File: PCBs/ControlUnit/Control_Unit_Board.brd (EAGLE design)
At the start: 78.7 x 65.7 mm, 14 parts, among them T1 2N2222, T2 2N2222

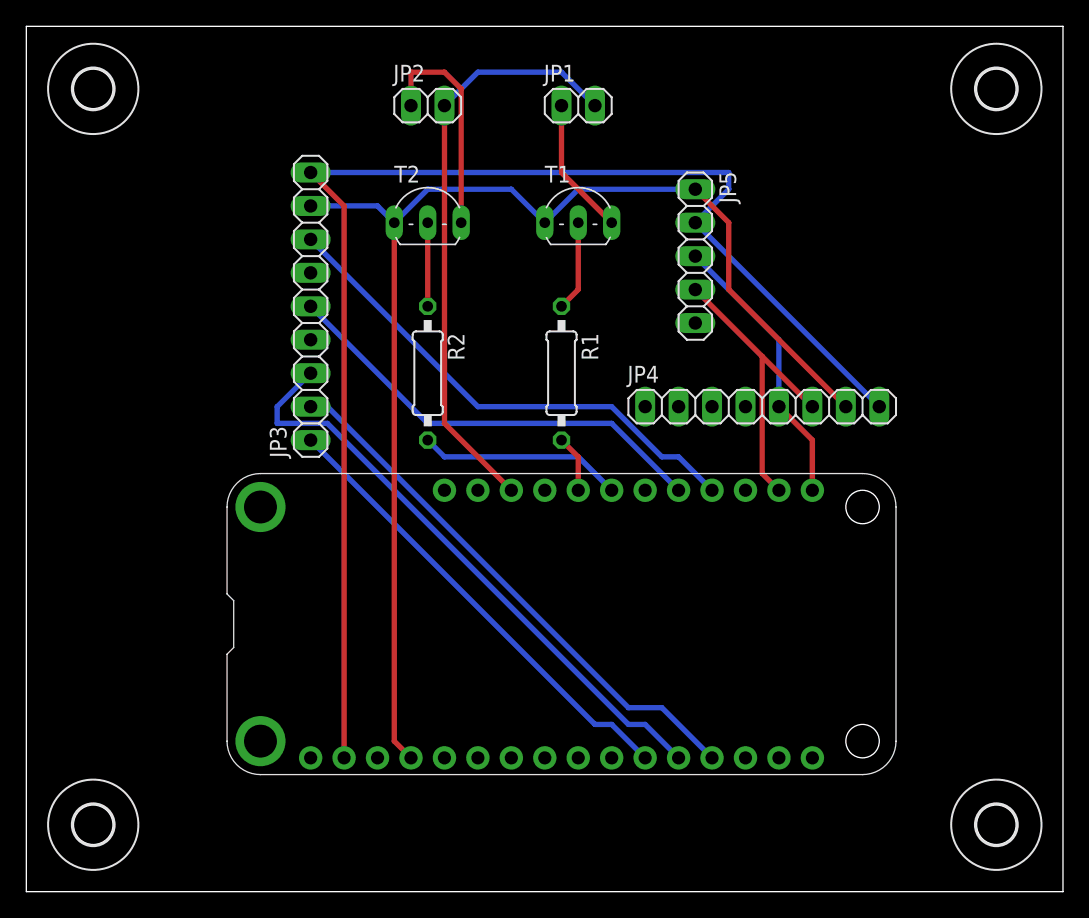
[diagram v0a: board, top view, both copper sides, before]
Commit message: Control Unit PCB finished, Sensor unit almost
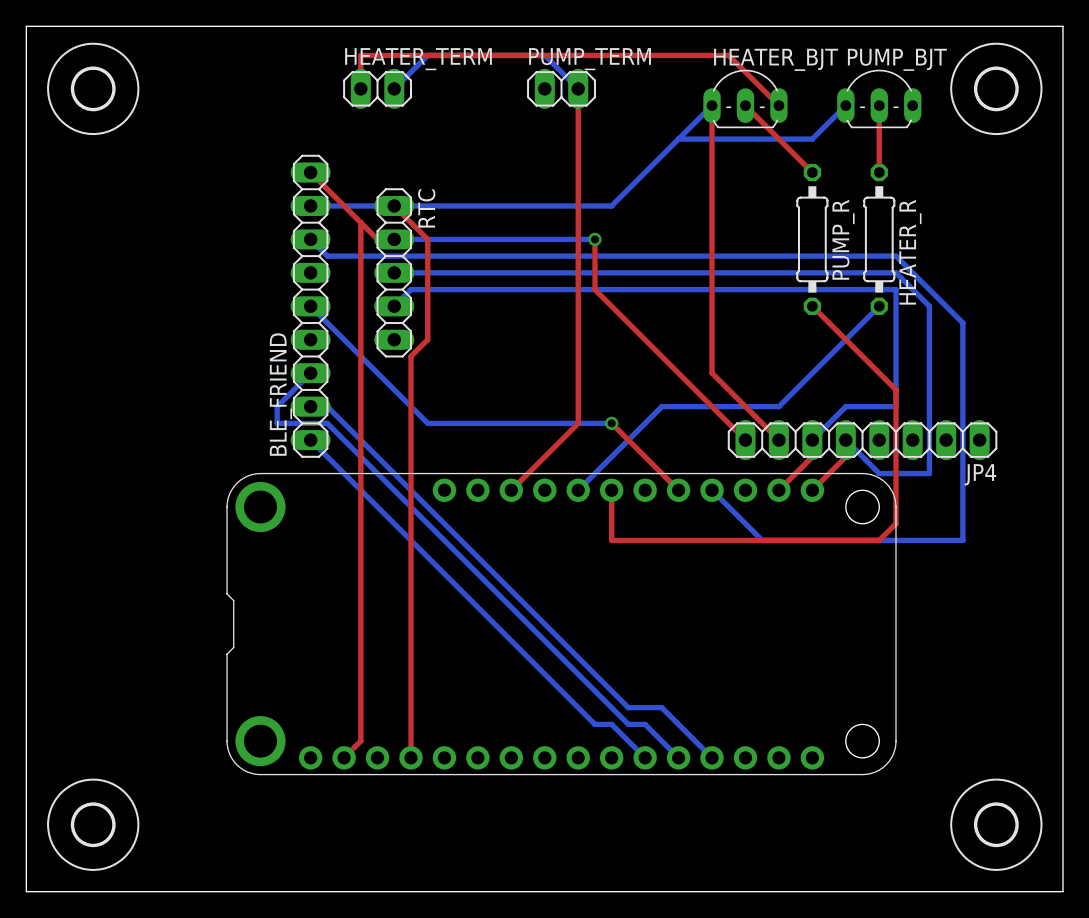
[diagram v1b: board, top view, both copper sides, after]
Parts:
- removed JP1, JP2: (no value), pinhead:1X02
- removed JP5: (no value), pinhead:1X05
- removed R1, R2: (no value), eagle-ltspice:0207/10
- removed T1, T2: 2N2222, adafruit:TO92-EBC-OVAL
- added HEATER_BJT, PUMP_BJT: 2N2222, adafruit:TO92-EBC-OVAL
- added HEATER_R, PUMP_R: (no value), eagle-ltspice:0207/10
- added HEATER_TERM, PUMP_TERM: (no value), pinhead:1X02
- added RTC: (no value), pinhead:1X05
- moved JP4 8.03 mm to (64.8, 71.1), turned to 180 degrees
- renumbered JP3 to BLE_FRIEND
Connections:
- new net S$1: PUMP_TERM.1
- net GND: now also HEATER_BJT.E, PUMP_BJT.E, RTC.1; no longer JP5.1, T1.E, T2.E
- net N$10: now also RTC.3; no longer JP5.3
- net N$11: now also PUMP_BJT.C; no longer JP1.1, T1.C
- net N$12: now also HEATER_BJT.C, HEATER_TERM.1; no longer JP2.1, T2.C
- net N$14: now also RTC.4; no longer JP5.4
- net N$6: now also PUMP_R.2; no longer R2.2
- net N$7: now also HEATER_R.2; no longer R1.2
- net N$8: now also HEATER_R.1, PUMP_BJT.B; no longer R1.1, T1.B
- net N$9: now also HEATER_BJT.B, PUMP_R.1; no longer R2.1, T2.B
- net USB: now also HEATER_TERM.2, PUMP_TERM.2; no longer JP1.2, JP2.2
- net VCC: now also RTC.2; no longer JP5.2
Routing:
- net N$15: track 38.4 -> 89.3 mm
- net N$10: track 21.5 -> 66.7 mm
- net N$14: track 23.3 -> 59.8 mm
- net N$6: track 15.5 -> 45.1 mm
- net N$7: track 4.34 -> 28.6 mm
- net GND: track 95.3 -> 118.4 mm
- net N$12: track 17.0 -> 35.9 mm
- net VCC: track 101.9 -> 84.8 mm, vias 0 -> 1
- net N$11: track 10.5 -> 0.00 mm
- net USB: track 44.8 -> 48.7 mm
- net N$8: track 6.88 -> 5.08 mm
- net N$9: track 6.35 -> 7.18 mm
- net N$5: vias 0 -> 1

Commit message: Update Control_Unit_Board.brd
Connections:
- removed net N$4: BLE_FRIEND.4
- net N$11: now also PUMP_TERM.1
- net S$1: now also BLE_FRIEND.4, MS1.22; no longer PUMP_TERM.1
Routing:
- net N$15: track 89.3 -> 53.4 mm
- net N$11: track 0.00 -> 31.6 mm
- net N$1: track 41.5 -> 72.6 mm
- net S$1: track 0.00 -> 30.1 mm
- net VCC: track 84.8 -> 108.9 mm, vias 1 -> 0
- net N$6: track 45.1 -> 28.5 mm
- net N$7: track 28.6 -> 37.0 mm
- net N$2: track 45.9 -> 41.2 mm
- net N$10: track 66.7 -> 69.9 mm
- net N$12: track 35.9 -> 34.4 mm
- net N$14: track 59.8 -> 58.3 mm
- net N$5: track 33.7 -> 34.5 mm, vias 1 -> 0
